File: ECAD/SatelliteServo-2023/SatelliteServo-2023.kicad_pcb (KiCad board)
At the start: 2 copper layers, 25 x 65 mm, 9 parts, among them J1 Conn_02x05_Odd_Even, J2 Conn_01x02

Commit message: New satellite Board
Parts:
- added J10: Conn_01x03, Footprints:PinHeader_3x01_P2.54mm_Horizontal, F.Cu at (143.0, 83.1)
- added J11: Conn_01x03, Footprints:PinHeader_3x01_P2.54mm_Horizontal, F.Cu at (143.0, 96.3)
- added J3: Conn_01x03, Footprints:PinHeader_3x01_P2.54mm_Horizontal, F.Cu at (141.2, 98.1)
- added J4: Conn_01x03, Footprints:PinHeader_3x01_P2.54mm_Horizontal, F.Cu at (141.5, 111.6)
- added J5: Conn_01x03, Footprints:PinHeader_3x01_P2.54mm_Horizontal, F.Cu at (139.7, 113.4)
- added J6: Conn_01x03, Footprints:PinHeader_3x01_P2.54mm_Horizontal, F.Cu at (143.3, 109.8)
- added J7: Conn_01x03, Footprints:PinHeader_3x01_P2.54mm_Horizontal, F.Cu at (141.2, 84.9)
- added J8: Conn_01x03, Footprints:PinHeader_3x01_P2.54mm_Horizontal, F.Cu at (139.4, 86.7)
- added J9: Conn_01x03, Footprints:PinHeader_3x01_P2.54mm_Horizontal, F.Cu at (139.4, 99.9)
- moved H2 30.0 mm to (139.1, 136.0)
- moved J1 16.7 mm to (152.6, 70.0), turned to -90 degrees
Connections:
- J1 pad 1: IO_1 -> IO_A_1
- J1 pad 10: IO_8 -> IO_P_2
- J1 pad 2: IO_2 -> IO_A_2
- J1 pad 3: IO_3 -> IO_D_2
- J1 pad 4: IO_4 -> IO_D_1
- J1 pad 5: IO_9 -> IO_D_3
- J1 pad 7: IO_5 -> IO_A_3
- J1 pad 8: IO_6 -> IO_A_4
- J1 pad 9: IO_7 -> IO_P_1
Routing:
- net IO_D_3: track 0.00 -> 68.5 mm
- net +5VP: track 18.6 -> 84.3 mm
- net IO_D_2: track 0.00 -> 59.1 mm
- net IO_A_1: track 0.00 -> 48.4 mm
- net IO_A_2: track 0.00 -> 37.9 mm
- net IO_D_1: track 0.00 -> 33.5 mm
- net IO_A_4: track 0.00 -> 30.0 mm
- net IO_P_2: track 0.00 -> 25.0 mm
- net IO_A_3: track 0.00 -> 24.9 mm
- net IO_P_1: track 0.00 -> 24.9 mm
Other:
- board size 25 x 65 mm -> 25 x 95 mm
- board text added: "+"

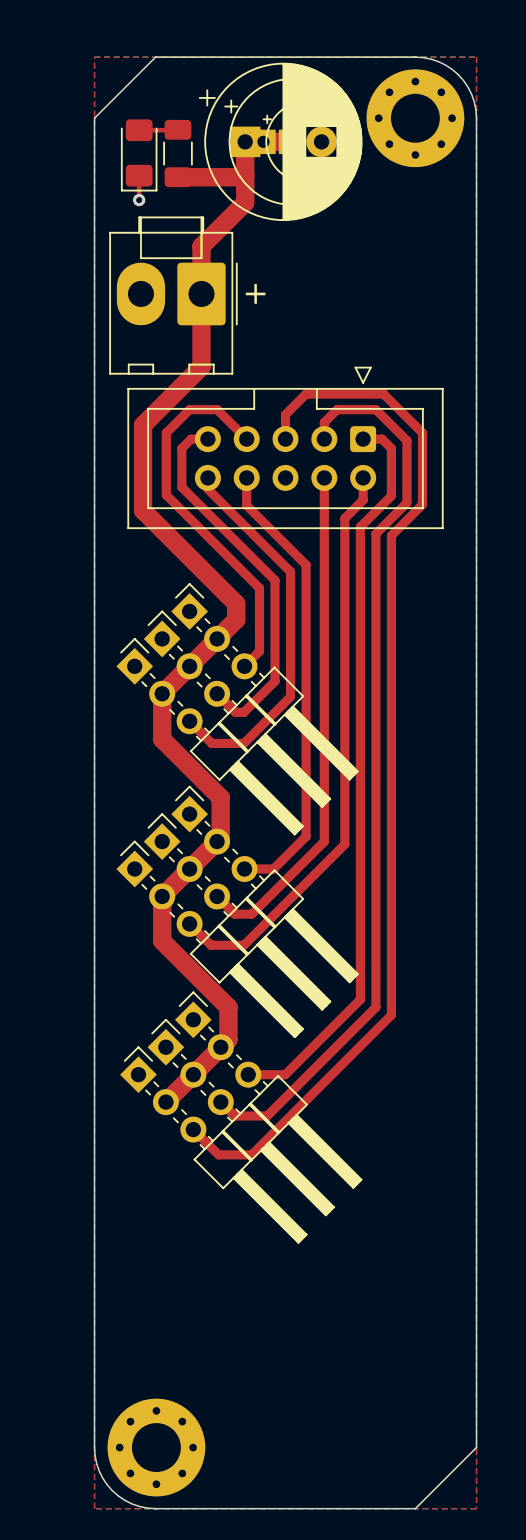
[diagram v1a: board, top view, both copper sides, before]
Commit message: Live 146 - Fix servo board
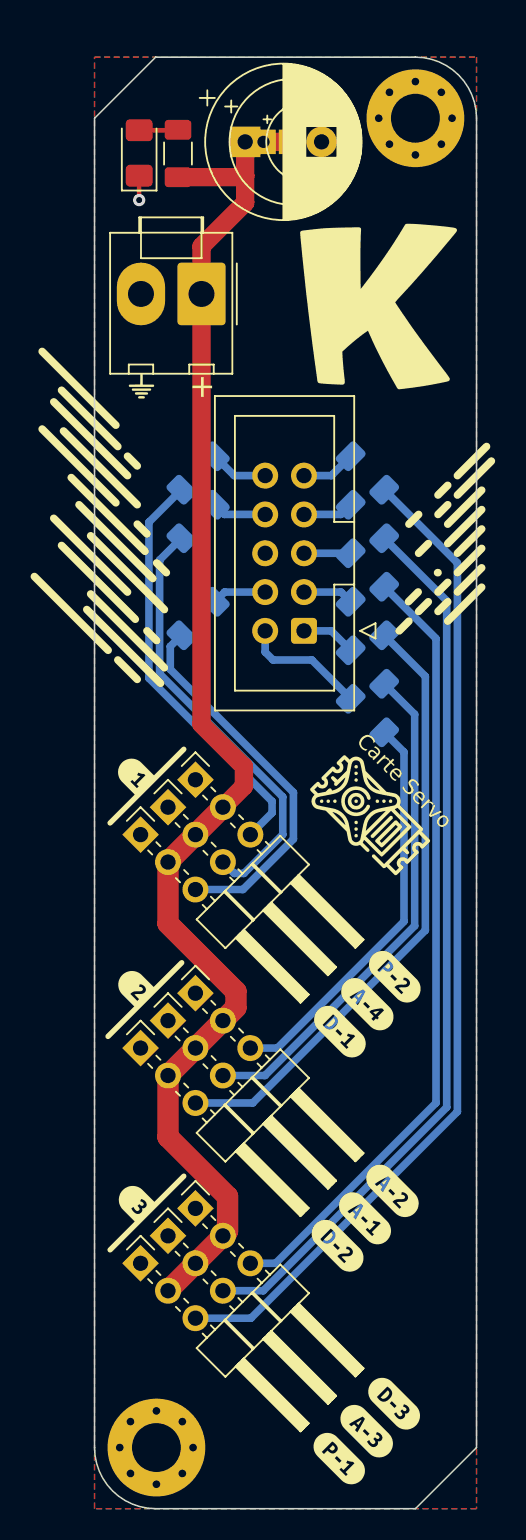
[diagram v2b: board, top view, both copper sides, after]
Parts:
- added G***: LOGO, LOGO, F.Cu at (138.1, 66.5)
- added G***: LOGO, LOGO, F.Cu at (153.0, 94.6)
- added G***: LOGO, LOGO, B.Cu at (156.8, 134.0)
- added G***: LOGO, LOGO, B.Cu at (138.0, 63.9)
- added G***: LOGO, LOGO, B.Cu at (143.6, 136.2)
- added G***: LOGO, LOGO, B.Cu at (155.9, 53.5)
- added G***: LOGO, LOGO, B.Cu at (149.8, 52.9)
- added G***: LOGO, LOGO, B.Cu at (143.9, 77.4)
- added G***: LOGO, LOGO, B.Cu at (153.7, 61.6)
- added R10: 220, Resistor_SMD:R_1206_3216Metric_Pad1.30x1.75mm_HandSolder, B.Cu at (141.8, 75.4)
- added R2: 220, Resistor_SMD:R_1206_3216Metric_Pad1.30x1.75mm_HandSolder, B.Cu at (141.8, 81.7)
- added R3: 220, Resistor_SMD:R_1206_3216Metric_Pad1.30x1.75mm_HandSolder, B.Cu at (152.9, 81.7)
- added R4: 220, Resistor_SMD:R_1206_3216Metric_Pad1.30x1.75mm_HandSolder, B.Cu at (152.9, 78.6)
- added R5: 220, Resistor_SMD:R_1206_3216Metric_Pad1.30x1.75mm_HandSolder, B.Cu at (152.9, 72.2)
- added R6: 220, Resistor_SMD:R_1206_3216Metric_Pad1.30x1.75mm_HandSolder, B.Cu at (141.8, 72.2)
- added R7: 220, Resistor_SMD:R_1206_3216Metric_Pad1.30x1.75mm_HandSolder, B.Cu at (152.9, 84.9)
- added R8: 220, Resistor_SMD:R_1206_3216Metric_Pad1.30x1.75mm_HandSolder, B.Cu at (152.9, 88.1)
- added R9: 220, Resistor_SMD:R_1206_3216Metric_Pad1.30x1.75mm_HandSolder, B.Cu at (152.9, 75.4)
- added kibuzzard-634F18D6: G***, kibuzzard-634F18D6, F.Cu at (154.7, 105.2)
- added kibuzzard-634F18D6: G***, kibuzzard-634F18D6, B.Cu at (147.9, 98.4)
- added kibuzzard-634F18FE: G***, kibuzzard-634F18FE, F.Cu at (152.9, 107.0)
- added kibuzzard-634F18FE: G***, kibuzzard-634F18FE, B.Cu at (146.1, 100.2)
- added kibuzzard-634F1907: G***, kibuzzard-634F1907, F.Cu at (151.1, 108.8)
- added kibuzzard-634F1907: G***, kibuzzard-634F1907, B.Cu at (144.3, 102.0)
- added kibuzzard-634F19A0: G***, kibuzzard-634F19A0, F.Cu at (154.5, 119.2)
- added kibuzzard-634F19A0: G***, kibuzzard-634F19A0, B.Cu at (147.9, 112.4)
- added kibuzzard-634F19A7: G***, kibuzzard-634F19A7, F.Cu at (152.7, 121.0)
- added kibuzzard-634F19A7: G***, kibuzzard-634F19A7, B.Cu at (146.1, 114.2)
- added kibuzzard-634F19AD: G***, kibuzzard-634F19AD, F.Cu at (150.9, 122.8)
- added kibuzzard-634F19AD: G***, kibuzzard-634F19AD, B.Cu at (144.3, 116.0)
- added kibuzzard-634F19FE: G***, kibuzzard-634F19FE, F.Cu at (154.6, 133.1)
- added kibuzzard-634F19FE: G***, kibuzzard-634F19FE, B.Cu at (147.6, 126.4)
- added kibuzzard-634F1A03: G***, kibuzzard-634F1A03, F.Cu at (152.8, 134.9)
- added kibuzzard-634F1A03: G***, kibuzzard-634F1A03, B.Cu at (145.8, 128.2)
- added kibuzzard-634F1A09: G***, kibuzzard-634F1A09, F.Cu at (151.0, 136.7)
- added kibuzzard-634F1A09: G***, kibuzzard-634F1A09, B.Cu at (144.0, 130.0)
- added kibuzzard-634F1B38: G***, kibuzzard-634F1B38, F.Cu at (137.6, 92.0)
- added kibuzzard-634F1B56: G***, kibuzzard-634F1B56, F.Cu at (137.6, 105.9)
- added kibuzzard-634F1B5B: G***, kibuzzard-634F1B5B, F.Cu at (137.6, 119.9)
- added kibuzzard-634F1BA4: G***, kibuzzard-634F1BA4, B.Cu at (137.6, 91.9)
- added kibuzzard-634F1BAB: G***, kibuzzard-634F1BAB, B.Cu at (137.6, 105.9)
- added kibuzzard-634F1BB2: G***, kibuzzard-634F1BB2, B.Cu at (137.6, 119.9)
- moved J7 40.9 mm to (139.8, 125.7)
- moved J10 40.9 mm to (141.6, 123.9)
- moved J1 13.1 mm to (148.7, 82.5), turned to 180 degrees
- moved J5 9.51 mm to (143.4, 122.1)
- moved J9 9.05 mm to (143.4, 108.1)
- moved J8 8.42 mm to (143.4, 94.1)
- moved J6 1.66 mm to (141.6, 109.9)
- moved J4 1.66 mm to (139.8, 111.7)
- moved J11 1.49 mm to (141.6, 95.9)
- moved J3 1.49 mm to (139.8, 97.7)
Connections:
- J10 pad 3: IO_A_3 -> Net-(J10-Pad3)
- J11 pad 3: IO_A_4 -> Net-(J11-Pad3)
- J3 pad 3: IO_D_1 -> Net-(J3-Pad3)
- J4 pad 3: IO_D_2 -> Net-(J4-Pad3)
- J5 pad 3: IO_D_3 -> Net-(J5-Pad3)
- J6 pad 3: IO_A_1 -> Net-(J6-Pad3)
- J7 pad 3: IO_P_1 -> Net-(J7-Pad3)
- J8 pad 3: IO_P_2 -> Net-(J8-Pad3)
- J9 pad 3: IO_A_2 -> Net-(J9-Pad3)
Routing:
- net IO_D_3: track 68.5 -> 3.06 mm
- net Net-(J7-Pad3): track 0.00 -> 65.4 mm
- net Net-(J10-Pad3): track 0.00 -> 58.6 mm
- net IO_D_2: track 59.1 -> 3.32 mm
- net Net-(J5-Pad3): track 0.00 -> 51.7 mm
- net IO_A_1: track 48.4 -> 3.58 mm
- net Net-(J4-Pad3): track 0.00 -> 40.2 mm
- net Net-(J6-Pad3): track 0.00 -> 33.3 mm
- net IO_D_1: track 33.5 -> 3.56 mm
- net IO_A_2: track 37.9 -> 8.42 mm
- net Net-(J11-Pad3): track 0.00 -> 28.6 mm
- net Net-(J8-Pad3): track 0.00 -> 27.4 mm
- net IO_A_4: track 30.0 -> 3.56 mm
- net Net-(J9-Pad3): track 0.00 -> 26.4 mm
- net Net-(J3-Pad3): track 0.00 -> 24.8 mm
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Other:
- board text added: "Barbatronic"
- board text added: "Carte Servo"
- board text added: "Karibous 2022-23"

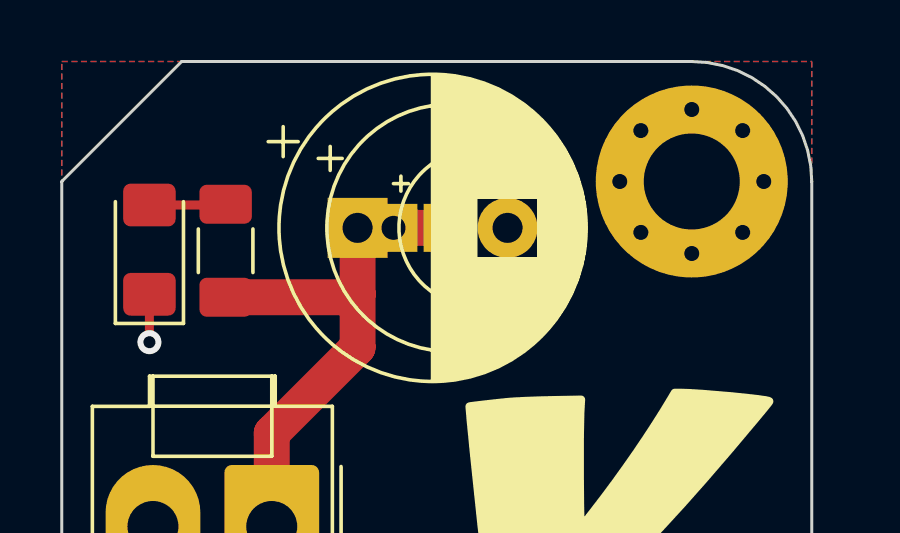
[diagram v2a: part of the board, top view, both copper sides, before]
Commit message: fix capacitor positions
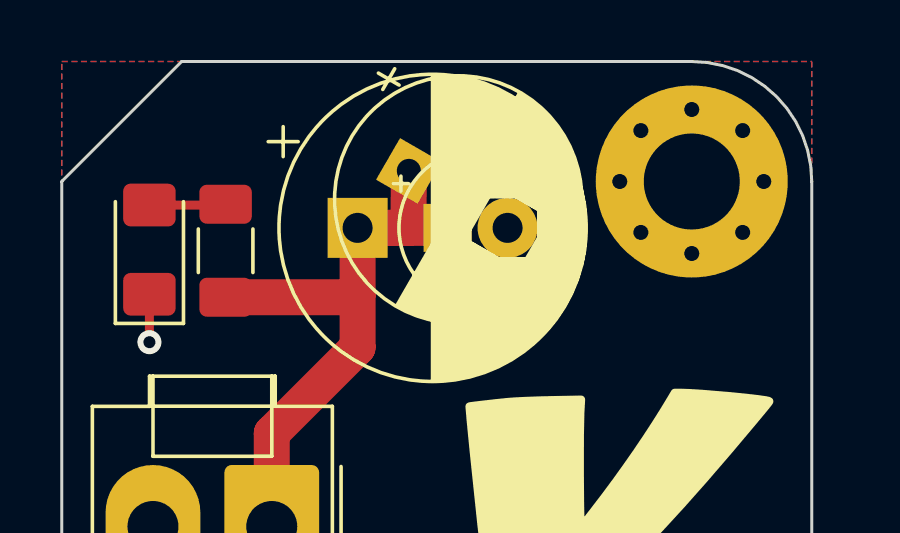
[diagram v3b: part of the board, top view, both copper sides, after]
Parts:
- moved C2 1.97 mm to (146.6, 48.6), turned to -30 degrees
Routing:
- net +5VP: track 93.9 -> 97.5 mm
